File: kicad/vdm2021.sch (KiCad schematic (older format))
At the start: 176 parts, among them IC1 7406, IC10 74LS109, IC11 74LS138, IC12 74LS86, IC13 74LS109, IC14 74LS02, IC15 74LS00, IC16 74LS109, IC17 74LS175, IC18 74LS132, IC19 74LS04, IC2 74LS163, IC20 74LS163, IC21 74LS163, IC22 74LS163, IC23 74LS157, IC24 74LS157, IC25 4049, IC26 4029, IC27 4029, IC28 74LS157, IC29 DM8131, IC3 74166, IC30 4001, IC31 4042, IC32 4042, IC33 74LS08, IC34 74LS08, IC35 74LS00, IC36 74LS04, IC37 8836, IC38 74LS367, IC39 74LS367, IC4 MCM6575, IC40 74LS10, IC41 2102, IC42 2102, IC43 2102, IC44 2102, IC45 2102, IC46 2102, IC47 2102, IC48 2102, IC49 L7805, IC5 74LS175, IC50 L7812, IC6 74LS175, IC7 74LS20, IC8 93L16, IC9 74LS10, J2 Jumper_3_Open, J4 Jumper_2_Open, J5 Jumper_2_Open, Q1 2N2907, SW1 SW_DIP_x06, Y1 Crystal

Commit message: Cleanup structure
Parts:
- ADDR1: footprint vdm2:ADDR_SELECT -> vdm2021:ADDR_SELECT; symbol vdm2:AddressSelect -> vdm2021:AddressSelect
- IC11: symbol vdm2:74LS138 -> vdm2021:74LS138
- IC17: symbol vdm2:74LS175-Units -> vdm2021:74LS175-Units
- IC2, IC21, IC22: symbol vdm2:74LS163-v2 -> vdm2021:74LS163-v2
- IC20: symbol vdm2:74LS163 -> vdm2021:74LS163
- IC23, IC28: symbol vdm2:74LS157-IC23 -> vdm2021:74LS157-IC23
- IC23, IC24: symbol vdm2:74LS157-IC24 -> vdm2021:74LS157-IC24
- IC26, IC27: symbol vdm2:4029 -> vdm2021:4029
- IC28: symbol vdm2:IC28 -> vdm2021:IC28
- IC29: symbol vdm2:DM8131 -> vdm2021:DM8131
- IC3: symbol vdm2:74166 -> vdm2021:74166
- IC31: symbol vdm2:4042 -> vdm2021:4042
- IC32: symbol vdm2:4042-IC32 -> vdm2021:4042-IC32
- IC37: symbol vdm2:8836 -> vdm2021:8836
- IC38, IC39: symbol vdm2:74LS367 -> vdm2021:74LS367
- IC4: symbol vdm2:MCM6575 -> vdm2021:MCM6575
- IC41, IC42, IC43, IC44, IC45, IC46, IC47, IC48: symbol vdm2:2102 -> vdm2021:2102
- IC49: footprint vdm2:TO-220-3_Horizontal_TabDown -> vdm2021:TO-220-3_Horizontal_TabDown
- IC5: symbol vdm2:IC5 -> vdm2021:IC5
- IC6: symbol vdm2:IC6 -> vdm2021:IC6
- IC8: symbol vdm2:93L16 -> vdm2021:93L16
- S100: footprint vdm2:S100_MALE -> vdm2021:S100_MALE; symbol vdm2:S100 -> vdm2021:S100
- SW1: symbol vdm2:SW_DIP_x06 -> vdm2021:SW_DIP_x06
- VIDEO1: footprint vdm2:bnc-5-16345033 -> vdm2021:bnc-5-16345033

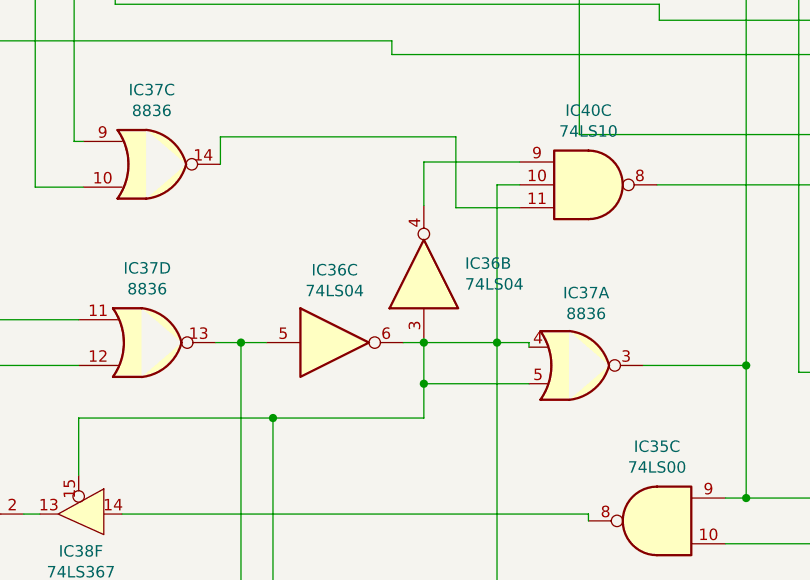
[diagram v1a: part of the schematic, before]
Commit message: Fix IC36 net in schematic
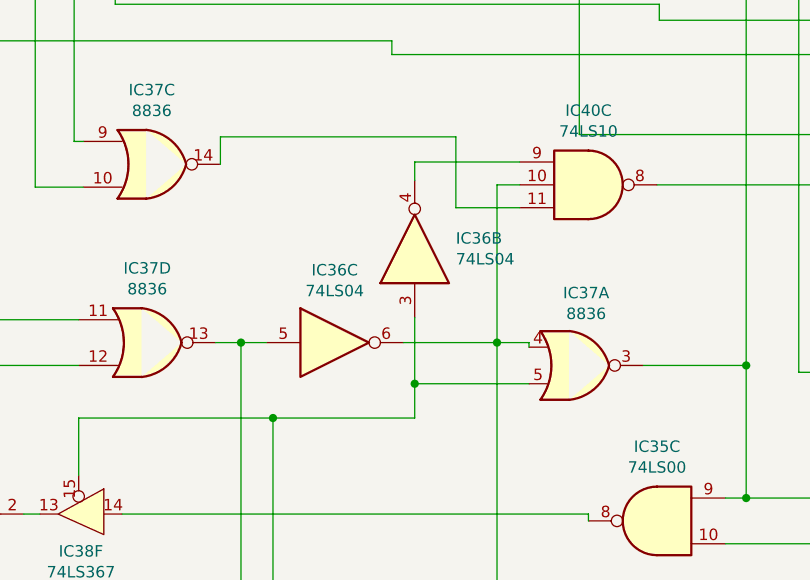
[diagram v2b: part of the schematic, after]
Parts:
- R33, R50: footprint Potentiometer_THT:Potentiometer_ACP_CA9-H2,5_Horizontal -> Potentiometer_THT:Potentiometer_Bourns_3339P_Vertical_HandSoldering
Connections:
- net at ADDR1.13, ADDR1.14, ADDR1.15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: no longer IC29.9, IC36.3, IC37.5, IC38.15
- new net: IC29.9, IC36.3, IC37.5, IC38.15
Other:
- moved on the sheet: IC36B
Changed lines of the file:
@@
 $Comp
 L 74xx:74LS04 IC36
-U 2 1 60D15BFF
-P 5640 14860
-F 0 "IC36" V 5686 14680 50  0000 R CNN
-F 1 "74LS04" V 5595 14680 50  0000 R CNN
-F 2 "Package_DIP:DIP-14_W7.62mm_Socket" H 5640 14860 50  0001 C CNN
-F 3 "http://www.ti.com/lit/gpn/sn74LS04" H 5640 14860 50  0001 C CNN
-	2    5640 14860
-	0    -1   -1   0
-$EndComp
-$Comp
-L 74xx:74LS04 IC36
 U 1 1 60D1E4CC
 P 9140 18140
@@
 	4980 17010 4980 15490
 Wire Wire Line
-	4980 15490 5640 15490
-Wire Wire Line
-	5640 15490 5640 15340
-Wire Wire Line
-	6100 15340 5640 15340
-Connection ~ 5640 15340
-Wire Wire Line
-	5640 15160 5640 15340
-Wire Wire Line
-	5550 15160 5640 15160
-Connection ~ 5640 15160
-Wire Wire Line
 	6100 15160 6100 15180
 Wire Wire Line
-	5640 15160 5960 15160
-Wire Wire Line
 	6060 14470 5960 14470
 Wire Wire Line
@@
 	5960 15160 6100 15160
 Wire Wire Line
-	6060 14370 5640 14370
-Wire Wire Line
-	5640 14370 5640 14560
-Wire Wire Line
 	6060 14570 5780 14570
 Wire Wire Line
@@
 Wire Wire Line
 	4130 15490 4980 15490
-Connection ~ 4980 15490
 Wire Wire Line
 	4320 15910 6360 15910
@@
 F 0 "R50" H 14061 14216 50  0000 R CNN
 F 1 "50K" H 14061 14125 50  0000 R CNN
-F 2 "Potentiometer_THT:Potentiometer_ACP_CA9-H2,5_Horizontal" H 14130 14170 50  0001 C CNN
+F 2 "Potentiometer_THT:Potentiometer_Bourns_3339P_Vertical_HandSoldering" H 14130 14170 50  0001 C CNN
 F 3 "~" H 14130 14170 50  0001 C CNN
 	1    14130 14170
@@
 F 0 "R33" H 14021 16796 50  0000 R CNN
 F 1 "50K" H 14021 16705 50  0000 R CNN
-F 2 "Potentiometer_THT:Potentiometer_ACP_CA9-H2,5_Horizontal" H 14090 16750 50  0001 C CNN
+F 2 "Potentiometer_THT:Potentiometer_Bourns_3339P_Vertical_HandSoldering" H 14090 16750 50  0001 C CNN
 F 3 "~" H 14090 16750 50  0001 C CNN
 	1    14090 16750
@@
 Wire Wire Line
 	28700 -450 29800 -450
+$Comp
+L 74xx:74LS04 IC36
+U 2 1 60D15BFF
+P 5600 14750
+F 0 "IC36" V 5646 14570 50  0000 R CNN
+F 1 "74LS04" V 5555 14570 50  0000 R CNN
+F 2 "Package_DIP:DIP-14_W7.62mm_Socket" H 5600 14750 50  0001 C CNN
+F 3 "http://www.ti.com/lit/gpn/sn74LS04" H 5600 14750 50  0001 C CNN
+	2    5600 14750
+	0    -1   -1   0
+$EndComp
+Wire Wire Line
+	5550 15160 5960 15160
+Wire Wire Line
+	5600 14370 5600 14450
+Wire Wire Line
+	5600 14370 6060 14370
+Wire Wire Line
+	4980 15490 5600 15490
+Wire Wire Line
+	5600 15490 5600 15340
+Connection ~ 4980 15490
+Wire Wire Line
+	6100 15340 5600 15340
+Connection ~ 5600 15340
+Wire Wire Line
+	5600 15340 5600 15050
 $EndSCHEMATC

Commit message: Routing updates after last schematic change
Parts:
- R33, R50: footprint Potentiometer_THT:Potentiometer_Bourns_3339P_Vertical_HandSoldering -> Potentiometer_THT:Potentiometer_ACP_CA9-H2,5_Horizontal
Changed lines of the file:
@@
 F 0 "R50" H 14061 14216 50  0000 R CNN
 F 1 "50K" H 14061 14125 50  0000 R CNN
-F 2 "Potentiometer_THT:Potentiometer_Bourns_3339P_Vertical_HandSoldering" H 14130 14170 50  0001 C CNN
+F 2 "Potentiometer_THT:Potentiometer_ACP_CA9-H2,5_Horizontal" H 14130 14170 50  0001 C CNN
 F 3 "~" H 14130 14170 50  0001 C CNN
 	1    14130 14170
@@
 F 0 "R33" H 14021 16796 50  0000 R CNN
 F 1 "50K" H 14021 16705 50  0000 R CNN
-F 2 "Potentiometer_THT:Potentiometer_Bourns_3339P_Vertical_HandSoldering" H 14090 16750 50  0001 C CNN
+F 2 "Potentiometer_THT:Potentiometer_ACP_CA9-H2,5_Horizontal" H 14090 16750 50  0001 C CNN
 F 3 "~" H 14090 16750 50  0001 C CNN
 	1    14090 16750

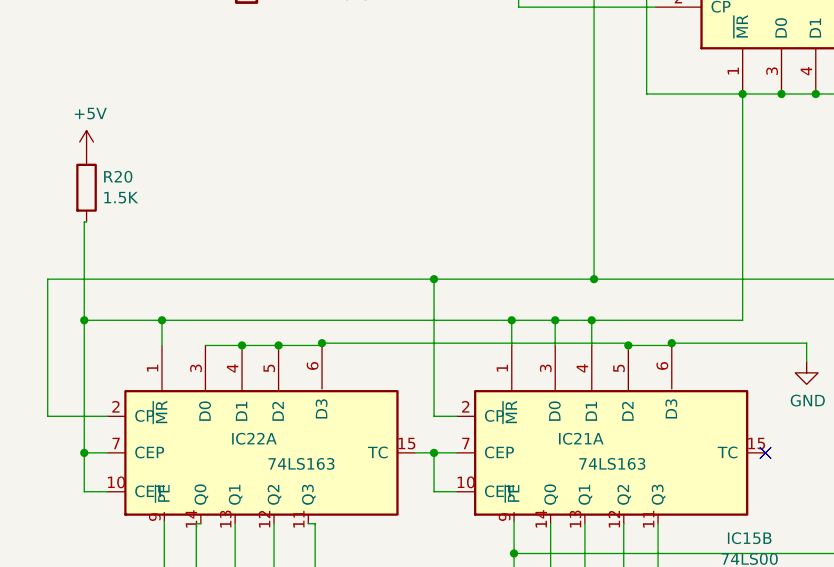
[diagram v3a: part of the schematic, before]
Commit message: Fixed IC22 load value
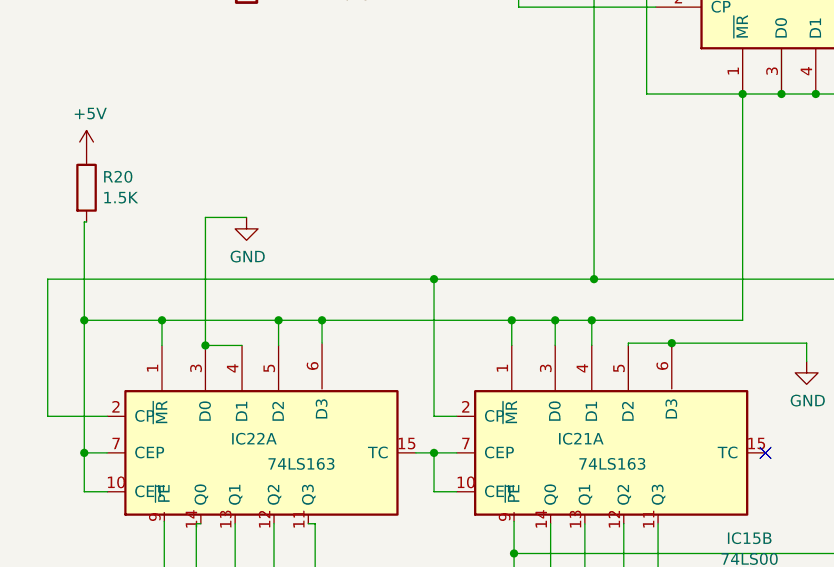
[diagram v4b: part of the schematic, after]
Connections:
- net GND: no longer IC22.5 (D2), IC22.6 (D3)
- net at IC20.1 (~MR), IC20.10 (CET), IC20.3 (D0)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: now also IC22.5 (D2), IC22.6 (D3)
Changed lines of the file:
@@
 	6110 5080 6110 5190
 Wire Wire Line
-	6270 5190 6460 5190
-Wire Wire Line
-	6460 5190 6460 5180
-Wire Wire Line
-	6460 5180 7050 5180
-Wire Wire Line
 	7050 5180 7050 5260
-Connection ~ 6460 5180
 $Comp
 L power:GND #PWR0105
@@
 $EndComp
 Wire Wire Line
-	4930 5180 6270 5180
-Wire Wire Line
-	6270 5180 6270 5190
-Connection ~ 6270 5190
-Wire Wire Line
-	4740 5190 4930 5190
-Wire Wire Line
-	4930 5190 4930 5180
-Connection ~ 4930 5180
-Connection ~ 4740 5190
-Wire Wire Line
 	4420 5190 4580 5190
-Connection ~ 4580 5190
-Wire Wire Line
-	4580 5190 4740 5190
 Wire Wire Line
 	4230 5190 4230 5080
 Connection ~ 4230 5080
 Wire Wire Line
-	4230 5080 5760 5080
+	4230 5080 4740 5080
 Wire Wire Line
 	5340 5660 5420 5660
@@
 Wire Wire Line
 	5600 15340 5600 15050
+Wire Wire Line
+	6460 5180 7050 5180
+Wire Wire Line
+	6460 5180 6270 5180
+Wire Wire Line
+	6270 5180 6270 5190
+Connection ~ 6460 5180
+$Comp
+L power:GND #PWR?
+U 1 1 6B9CA023
+P 4600 4630
+F 0 "#PWR?" H 4600 4380 50  0001 C CNN
+F 1 "GND" H 4605 4457 50  0000 C CNN
+F 2 "" H 4600 4630 50  0001 C CNN
+F 3 "" H 4600 4630 50  0001 C CNN
+	1    4600 4630
+	1    0    0    -1
+$EndComp
+Wire Wire Line
+	4420 5190 4420 4630
+Wire Wire Line
+	4420 4630 4600 4630
+Connection ~ 4420 5190
+Wire Wire Line
+	4740 5190 4740 5080
+Connection ~ 4740 5080
+Wire Wire Line
+	4740 5080 4930 5080
+Wire Wire Line
+	4930 5180 4930 5080
+Connection ~ 4930 5080
+Wire Wire Line
+	4930 5080 5760 5080
 $EndSCHEMATC

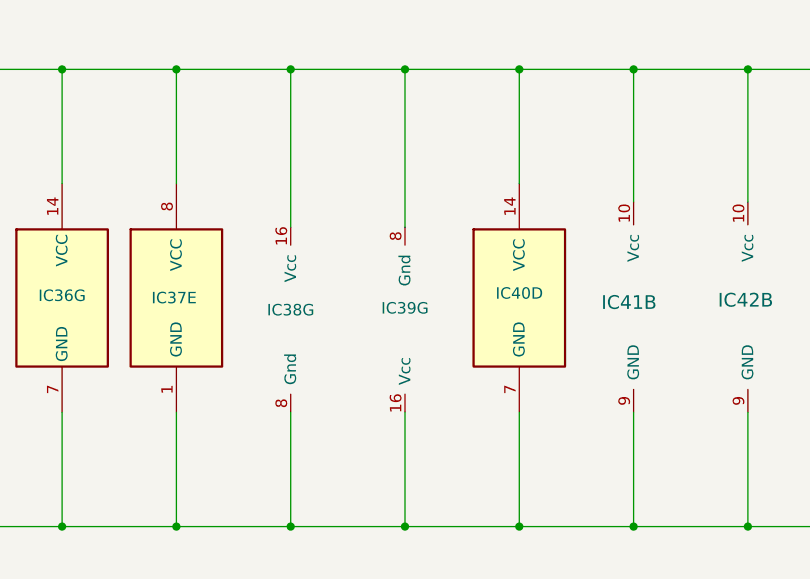
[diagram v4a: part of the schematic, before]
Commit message: Fixed IC39 Gnd/pwr swap
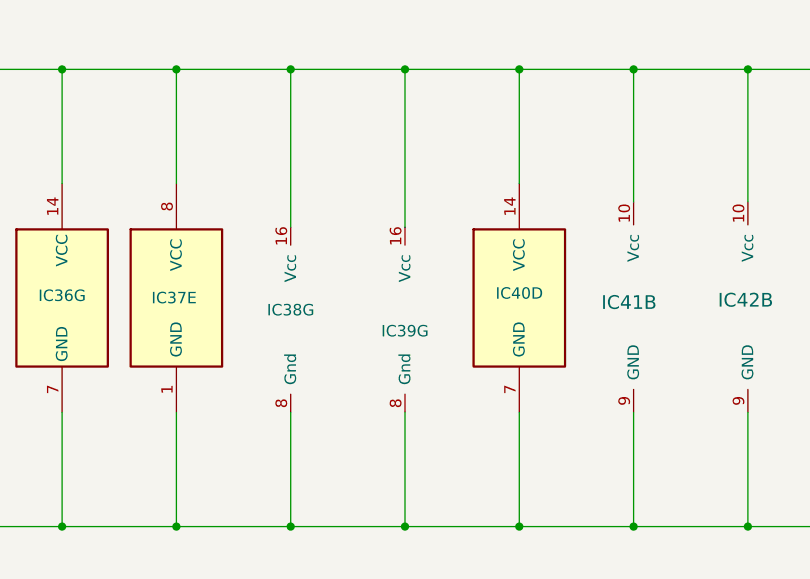
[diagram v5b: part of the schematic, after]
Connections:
- net +5V: now also IC39.16 (Vcc); no longer IC39.8 (Gnd)
- net GND: now also IC39.8 (Gnd); no longer IC39.16 (Vcc)
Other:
- moved on the sheet: IC39G
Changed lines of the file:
@@
 L vdm2021:74LS367 IC39
 U 7 1 62D34CF5
-P 20500 -1990
-F 0 "IC39" H 20500 -1955 50  0000 C CNN
-F 1 "74LS367" H 20500 -1864 50  0001 C CNN
-F 2 "Package_DIP:DIP-16_W7.62mm_Socket" H 20500 -1990 50  0001 C CNN
-F 3 "http://www.ti.com/lit/gpn/sn74LS367" H 20500 -1990 50  0001 C CNN
-	7    20500 -1990
-	1    0    0    1
+P 20500 -1820
+F 0 "IC39" H 20500 -1785 50  0000 C CNN
+F 1 "74LS367" H 20500 -1694 50  0001 C CNN
+F 2 "Package_DIP:DIP-16_W7.62mm_Socket" H 20500 -1820 50  0001 C CNN
+F 3 "http://www.ti.com/lit/gpn/sn74LS367" H 20500 -1820 50  0001 C CNN
+	7    20500 -1820
+	1    0    0    -1
 $EndComp
 $Comp
@@
 Wire Wire Line
 	20000 -3000 20500 -3000
-Wire Wire Line
-	20500 -2310 20500 -3000
 Connection ~ 20500 -3000
 Wire Wire Line
@@
 Connection ~ 6460 5180
 $Comp
-L power:GND #PWR?
+L power:GND #PWR0167
 U 1 1 6B9CA023
 P 4600 4630
-F 0 "#PWR?" H 4600 4380 50  0001 C CNN
+F 0 "#PWR0167" H 4600 4380 50  0001 C CNN
 F 1 "GND" H 4605 4457 50  0000 C CNN
 F 2 "" H 4600 4630 50  0001 C CNN
@@
 Wire Wire Line
 	4930 5080 5760 5080
+Wire Wire Line
+	20500 -3000 20500 -2310
 $EndSCHEMATC

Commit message: Fix Q1 pinout
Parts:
- Q1: symbol Device:Q_PNP_BCE -> Device:Q_PNP_EBC
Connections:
- net +5V: now also Q1.2 (B); no longer Q1.1 (B)
- net at IC13.6 (Q), IC27.1 (PE): no longer IC7.4, IC9.11
- net at C34.1, IC30.11: now also Q1.3 (C); no longer Q1.2 (C)
- net at C34.2, IC25.5, R24.2: now also Q1.1 (E); no longer Q1.3 (E)
- net at IC13.7 (~Q): now also IC7.4, IC9.11
- no-connect marks 22 -> 21
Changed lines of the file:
@@
 	13850 18780 16550 18780
 Wire Wire Line
-	16550 18780 16550 16790
-Wire Wire Line
 	16550 16790 16380 16790
 Wire Wire Line
@@
 	21610 15060 21610 14310
 $Comp
-L Device:Q_PNP_BCE Q1
+L Device:Q_PNP_EBC Q1
 U 1 1 63BD7E61
 P 11780 4070
@@
 	18970 16920 18970 18800
 Wire Wire Line
-	19080 16760 16550 16760
-Wire Wire Line
-	16550 16760 16550 16790
-Connection ~ 19080 16760
-Connection ~ 16550 16790
-NoConn ~ 16380 16990
-Wire Wire Line
 	18060 17120 17460 17120
 Wire Wire Line
@@
 Wire Wire Line
 	20500 -3000 20500 -2310
+Wire Wire Line
+	16550 16790 16550 18780
+Wire Wire Line
+	16380 16990 16660 16990
+Wire Wire Line
+	16660 16990 16660 16760
+Wire Wire Line
+	16660 16760 19080 16760
+Connection ~ 19080 16760
 $EndSCHEMATC

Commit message: Updated silkscreen URL.  Increased footprint size of R6 half watt resistor
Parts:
- R6: footprint Resistor_THT:R_Axial_DIN0207_L6.3mm_D2.5mm_P7.62mm_Horizontal -> Resistor_THT:R_Axial_DIN0207_L6.3mm_D2.5mm_P10.16mm_Horizontal
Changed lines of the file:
@@
 F 0 "R6" V 29153 16070 50  0000 C CNN
 F 1 "680" V 29244 16070 50  0000 C CNN
-F 2 "Resistor_THT:R_Axial_DIN0207_L6.3mm_D2.5mm_P7.62mm_Horizontal" V 29290 16070 50  0001 C CNN
+F 2 "Resistor_THT:R_Axial_DIN0207_L6.3mm_D2.5mm_P10.16mm_Horizontal" V 29290 16070 50  0001 C CNN
 F 3 "~" H 29360 16070 50  0001 C CNN
 	1    29360 16070
